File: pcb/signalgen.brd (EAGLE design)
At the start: 68.6 x 43.2 mm, 30 parts, among them U1 MSP430G2553, U2 TL974IN, U3 TLV4112CP, U4 LD1117-PTH, X1 MST2V, X2 MKDSN1,5/2-5,08

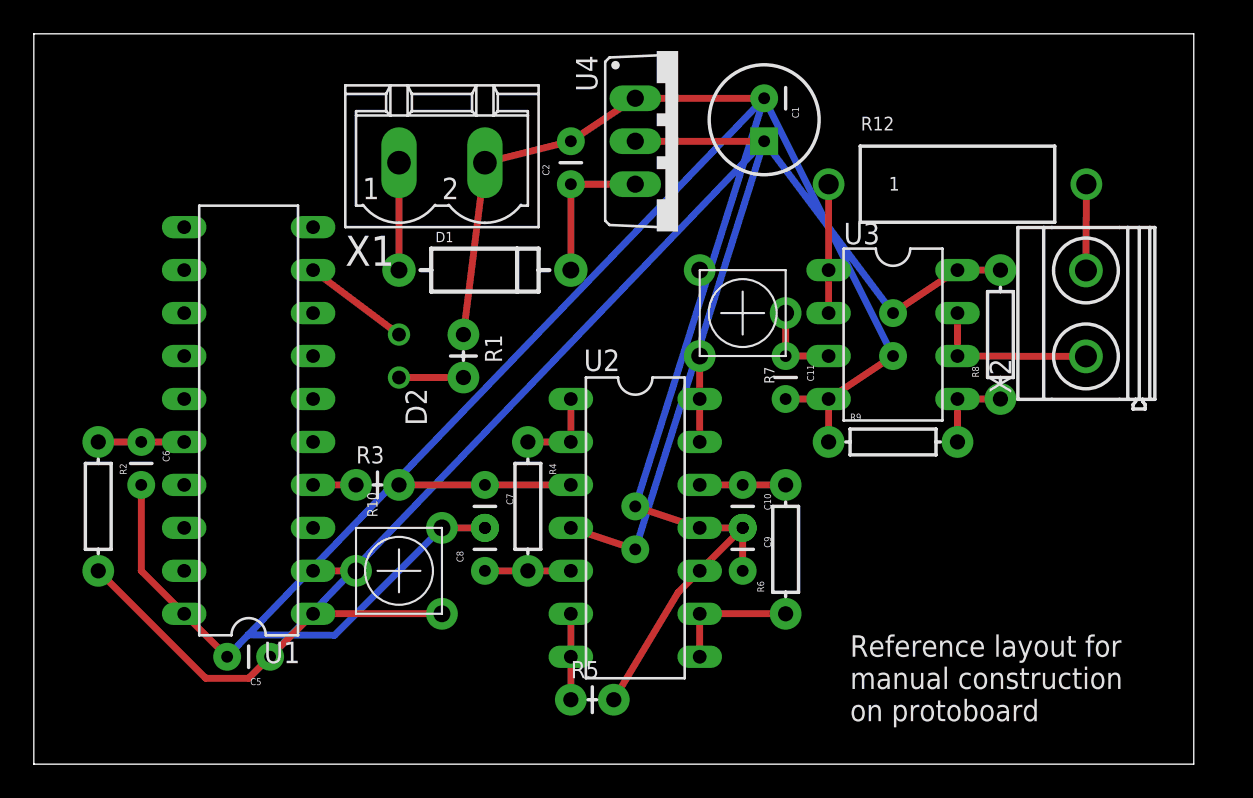
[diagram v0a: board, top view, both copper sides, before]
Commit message: Implemented system linearization
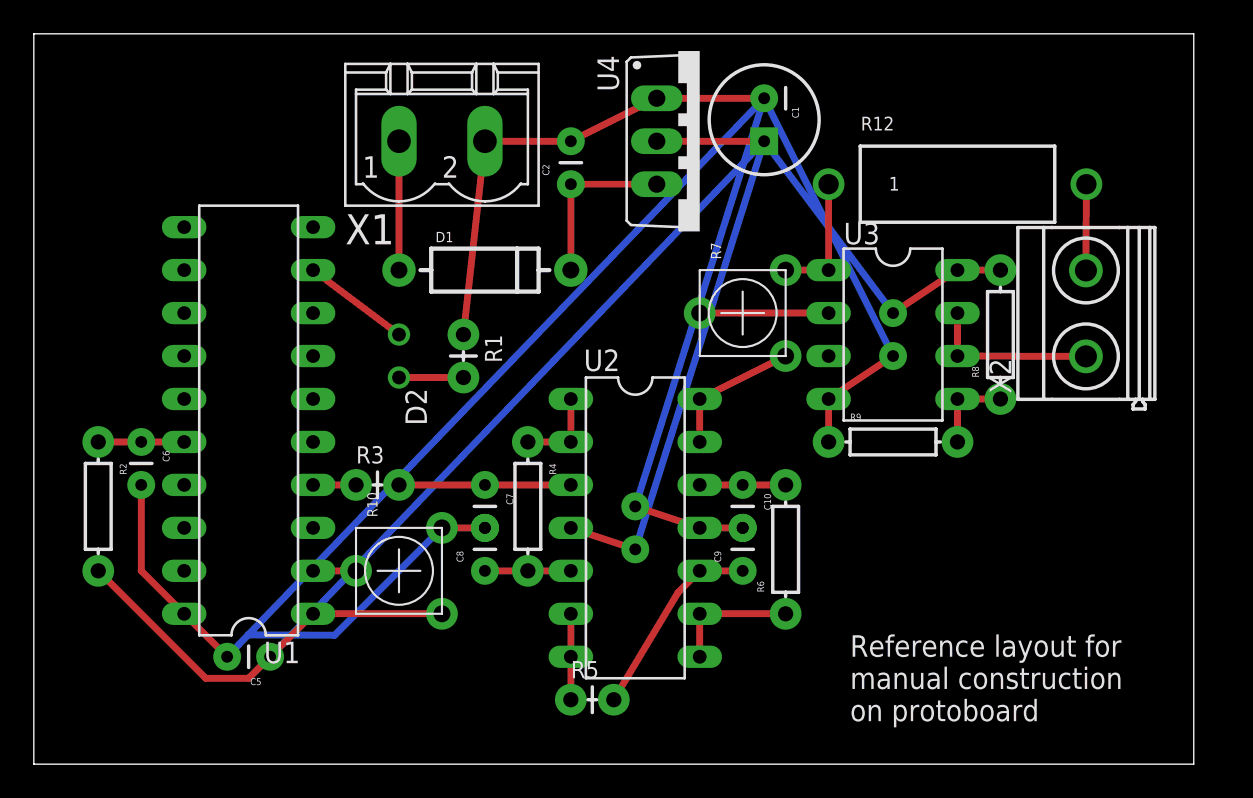
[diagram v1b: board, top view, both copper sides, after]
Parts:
- removed C11: 2.2nF, SparkFun-Capacitors:CAP-PTH-SMALL
- moved C9 2.54 mm to (41.9, 11.4), turned to 90 degrees
- moved U4 1.27 mm to (36.8, 36.8)
- moved X1 1.27 mm to (24.1, 36.8)
- turned R7 to 90 degrees
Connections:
- net GND: no longer C11.2
- net N$14: now also R7.1; no longer R7.3
- net N$15: now also U3.3
- net N$16: now also R7.3; no longer U3.2
- net N$18: now also U3.2; no longer C11.1, U3.3
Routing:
- net GND: track 163.5 -> 159.3 mm
- net N$14: track 5.08 -> 8.22 mm
- net N$18: track 5.08 -> 7.62 mm
- net N$2: track 8.89 -> 10.2 mm
- net N$1: track 6.35 -> 7.62 mm
- net 3.3V: track 123.5 -> 122.2 mm
- net N$12: track 12.8 -> 11.7 mm
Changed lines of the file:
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@@
 <element name="C7" library="SparkFun-Capacitors" package="CAP-PTH-SMALL" value="2.2nF" x="26.67" y="16.51" rot="R270"/>
 <element name="C8" library="SparkFun-Capacitors" package="CAP-PTH-SMALL" value="2.2nF" x="26.67" y="11.43" rot="R90"/>
-<element name="C9" library="SparkFun-Capacitors" package="CAP-PTH-SMALL" value="2.2nF" x="41.91" y="13.97" rot="R270"/>
+<element name="C9" library="SparkFun-Capacitors" package="CAP-PTH-SMALL" value="2.2nF" x="41.91" y="11.43" rot="R90"/>
 <element name="D1" library="SparkFun-DiscreteSemi" package="DIODE-1N4001" value="" x="26.67" y="29.21"/>
 <element name="D2" library="SparkFun-LED" package="LED3MM-NS" value="" x="21.59" y="24.13" rot="R270"/>
@@
 <element name="U2" library="Custom" package="DIP-14" value="TL974IN" x="35.56" y="13.97" rot="R270"/>
 <element name="U3" library="Custom" package="DIP-8" value="TLV4112CP" x="50.8" y="25.4" rot="R270"/>
-<element name="U4" library="Custom" package="TO-220ABS" value="LD1117-PTH" x="35.56" y="36.83" rot="R270"/>
-<element name="X1" library="con-phoenix-508" package="MSTBV2" value="MST2V" x="24.13" y="35.56">
-<attribute name="OC_NEWARK" value="unknown" x="24.13" y="35.56" size="1.778" layer="27" display="off"/>
-<attribute name="MPN" value="" x="24.13" y="35.56" size="1.778" layer="27" display="off"/>
-<attribute name="MF" value="" x="24.13" y="35.56" size="1.778" layer="27" display="off"/>
-<attribute name="OC_FARNELL" value="unknown" x="24.13" y="35.56" size="1.778" layer="27" display="off"/>
+<element name="U4" library="Custom" package="TO-220ABS" value="LD1117-PTH" x="36.83" y="36.83" rot="R270"/>
+<element name="X1" library="con-phoenix-508" package="MSTBV2" value="MST2V" x="24.13" y="36.83">
+<attribute name="OC_NEWARK" value="unknown" x="24.13" y="36.83" size="1.778" layer="27" display="off"/>
+<attribute name="MPN" value="" x="24.13" y="36.83" size="1.778" layer="27" display="off"/>
+<attribute name="MF" value="" x="24.13" y="36.83" size="1.778" layer="27" display="off"/>
+<attribute name="OC_FARNELL" value="unknown" x="24.13" y="36.83" size="1.778" layer="27" display="off"/>
 </element>
 <element name="X2" library="con-phoenix-508" package="MKDSN1,5/2-5,08" value="MKDSN1,5/2-5,08" x="62.23" y="26.67" rot="R90"/>
@@
 <attribute name="VALUE" value="1K" x="44.45" y="12.7" size="1.778" layer="27" rot="R90" display="off"/>
 </element>
-<element name="R7" library="SparkFun-Electromechanical" package="TRIM_POT_PTH" value="5K" x="41.91" y="26.67" rot="R270"/>
-<element name="C11" library="SparkFun-Capacitors" package="CAP-PTH-SMALL" value="2.2nF" x="44.45" y="24.13" rot="R270"/>
+<element name="R7" library="SparkFun-Electromechanical" package="TRIM_POT_PTH" value="5K" x="41.91" y="26.67" rot="R90"/>
 <element name="R8" library="SparkFun-Resistors" package="AXIAL-0.3" value="47K" x="57.15" y="25.4" rot="R90">
 <attribute name="PROD_ID" value="RES-12182" x="57.15" y="25.4" size="1.778" layer="27" rot="R90" display="off"/>
@@
 <contactref element="R10" pad="3"/>
 <contactref element="C10" pad="2"/>
-<contactref element="C11" pad="2"/>
 <contactref element="R9" pad="P$1"/>
-<wire x1="26.67" y1="35.56" x2="25.4" y2="25.4" width="0.4064" layer="1"/>
-<wire x1="31.75" y1="36.83" x2="35.56" y2="39.37" width="0.4064" layer="1"/>
+<wire x1="26.67" y1="36.83" x2="25.4" y2="25.4" width="0.4064" layer="1"/>
+<wire x1="31.75" y1="36.83" x2="36.83" y2="39.37" width="0.4064" layer="1"/>
 <wire x1="11.43" y1="6.35" x2="8.89" y2="8.89" width="0.4064" layer="1"/>
-<wire x1="41.91" y1="13.97" x2="41.91" y2="11.43" width="0.4064" layer="1"/>
 <wire x1="46.99" y1="19.05" x2="46.99" y2="21.59" width="0.4064" layer="1"/>
-<wire x1="46.99" y1="21.59" x2="44.45" y2="21.59" width="0.4064" layer="1"/>
 <wire x1="39.37" y1="13.97" x2="41.91" y2="13.97" width="0.4064" layer="1"/>
 <wire x1="35.56" y1="15.24" x2="39.37" y2="13.97" width="0.4064" layer="1"/>
@@
 <wire x1="6.35" y1="16.51" x2="6.35" y2="11.43" width="0.4064" layer="1"/>
 <wire x1="6.35" y1="11.43" x2="8.89" y2="8.89" width="0.4064" layer="1"/>
-<wire x1="26.67" y1="35.56" x2="31.75" y2="36.83" width="0.4064" layer="1"/>
+<wire x1="26.67" y1="36.83" x2="31.75" y2="36.83" width="0.4064" layer="1"/>
 <wire x1="43.18" y1="39.37" x2="12.67461875" y2="7.644403125" width="0.4064" layer="16"/>
 <wire x1="12.67461875" y1="7.644403125" x2="11.43" y2="6.35" width="0.4064" layer="16"/>
 <wire x1="43.18" y1="39.37" x2="35.56" y2="15.24" width="0.4064" layer="16"/>
 <wire x1="43.18" y1="39.37" x2="50.8" y2="24.13" width="0.4064" layer="16"/>
-<wire x1="43.18" y1="39.37" x2="35.56" y2="39.37" width="0.4064" layer="1"/>
+<wire x1="43.18" y1="39.37" x2="36.83" y2="39.37" width="0.4064" layer="1"/>
 <wire x1="24.13" y1="13.97" x2="26.67" y2="13.97" width="0.4064" layer="1"/>
 <wire x1="24.13" y1="13.97" x2="17.78" y2="7.62" width="0.4064" layer="16"/>
@@
 <contactref element="X1" pad="1"/>
 <contactref element="D1" pad="A"/>
-<wire x1="21.59" y1="29.21" x2="21.59" y2="35.56" width="0.4064" layer="1"/>
+<wire x1="21.59" y1="29.21" x2="21.59" y2="36.83" width="0.4064" layer="1"/>
 </signal>
 <signal name="N$2">
@@
 <contactref element="U4" pad="3"/>
 <contactref element="C2" pad="1"/>
-<wire x1="35.56" y1="34.29" x2="31.75" y2="34.29" width="0.4064" layer="1"/>
+<wire x1="36.83" y1="34.29" x2="31.75" y2="34.29" width="0.4064" layer="1"/>
 <wire x1="31.75" y1="34.29" x2="31.75" y2="29.21" width="0.4064" layer="1"/>
 </signal>
@@
 <contactref element="R10" pad="1"/>
 <contactref element="R8" pad="P$2"/>
-<wire x1="35.56" y1="36.83" x2="43.18" y2="36.83" width="0.4064" layer="1"/>
+<wire x1="36.83" y1="36.83" x2="43.18" y2="36.83" width="0.4064" layer="1"/>
 <wire x1="13.97" y1="6.35" x2="16.51" y2="8.89" width="0.4064" layer="1"/>
 <wire x1="57.15" y1="29.21" x2="54.61" y2="29.21" width="0.4064" layer="1"/>
@@
 <contactref element="C9" pad="1"/>
 <contactref element="U2" pad="10"/>
-<wire x1="39.37" y1="11.43" x2="41.91" y2="13.97" width="0.4064" layer="1"/>
+<wire x1="39.37" y1="11.43" x2="41.91" y2="11.43" width="0.4064" layer="1"/>
 <wire x1="34.29" y1="3.81" x2="38.1" y2="10.16" width="0.4064" layer="1"/>
 <wire x1="38.1" y1="10.16" x2="39.37" y2="11.43" width="0.4064" layer="1"/>
@@
 </signal>
 <signal name="N$16">
-<contactref element="U3" pad="2"/>
 <contactref element="U3" pad="1"/>
 <contactref element="R12" pad="P$1"/>
-<wire x1="46.99" y1="26.67" x2="46.99" y2="29.21" width="0.4064" layer="1"/>
 <wire x1="46.99" y1="29.21" x2="46.99" y2="34.29" width="0.4064" layer="1"/>
+<contactref element="R7" pad="3"/>
+<wire x1="44.45" y1="29.21" x2="46.99" y2="29.21" width="0.4064" layer="1"/>
 </signal>
 <signal name="N$17">
@@
 <contactref element="U2" pad="13"/>
 <contactref element="U2" pad="14"/>
-<contactref element="R7" pad="3"/>
 <wire x1="39.37" y1="19.05" x2="39.37" y2="21.59" width="0.4064" layer="1"/>
-<wire x1="39.37" y1="21.59" x2="39.37" y2="24.13" width="0.4064" layer="1"/>
+<contactref element="R7" pad="1"/>
+<wire x1="39.37" y1="21.59" x2="44.45" y2="24.13" width="0.4064" layer="1"/>
 </signal>
 <signal name="N$15">
-<contactref element="U3" pad="5"/>
 <contactref element="R8" pad="P$1"/>
 <contactref element="R9" pad="P$2"/>
-<wire x1="54.61" y1="19.05" x2="54.61" y2="21.59" width="0.4064" layer="1"/>
-<wire x1="54.61" y1="21.59" x2="57.15" y2="21.59" width="0.4064" layer="1"/>
-</signal>
-<signal name="N$18">
-<contactref element="R7" pad="2"/>
-<contactref element="C11" pad="1"/>
+<contactref element="U3" pad="5"/>
 <contactref element="U3" pad="3"/>
-<wire x1="46.99" y1="24.13" x2="44.45" y2="24.13" width="0.4064" layer="1"/>
-<wire x1="44.45" y1="24.13" x2="44.45" y2="26.67" width="0.4064" layer="1"/>
+<wire x1="57.15" y1="21.59" x2="54.61" y2="21.59" width="0.4064" layer="1"/>
+<wire x1="54.61" y1="21.59" x2="54.61" y2="19.05" width="0.4064" layer="1"/>
+<wire x1="46.99" y1="24.13" x2="54.61" y2="21.59" width="0" layer="19" extent="1-1"/>
 </signal>
 <signal name="N$11">
@@
 <wire x1="16.51" y1="29.21" x2="21.59" y2="25.4" width="0.4064" layer="1"/>
 </signal>
+<signal name="N$18">
+<contactref element="U3" pad="2"/>
+<contactref element="R7" pad="2"/>
+<wire x1="39.37" y1="26.67" x2="46.99" y2="26.67" width="0.4064" layer="1"/>
+</signal>
 </signals>
